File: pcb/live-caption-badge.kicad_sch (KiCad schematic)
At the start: 35 parts, among them J1 Conn_01x09, J2 Conn_01x04_Socket, J3 Conn_01x09, J5 USB_C_Receptacle_USB2.0_16P, J6 Conn_01x06, J7 Conn_01x03, SW1 SW_DPDT_x2, SW2 RST, SW3 BTN, SW4 BTN, SW5 BTN, U1 ESP32-S3-WROOM-1, U2 HE9073A33M5R, U3 HE9073A33M5R

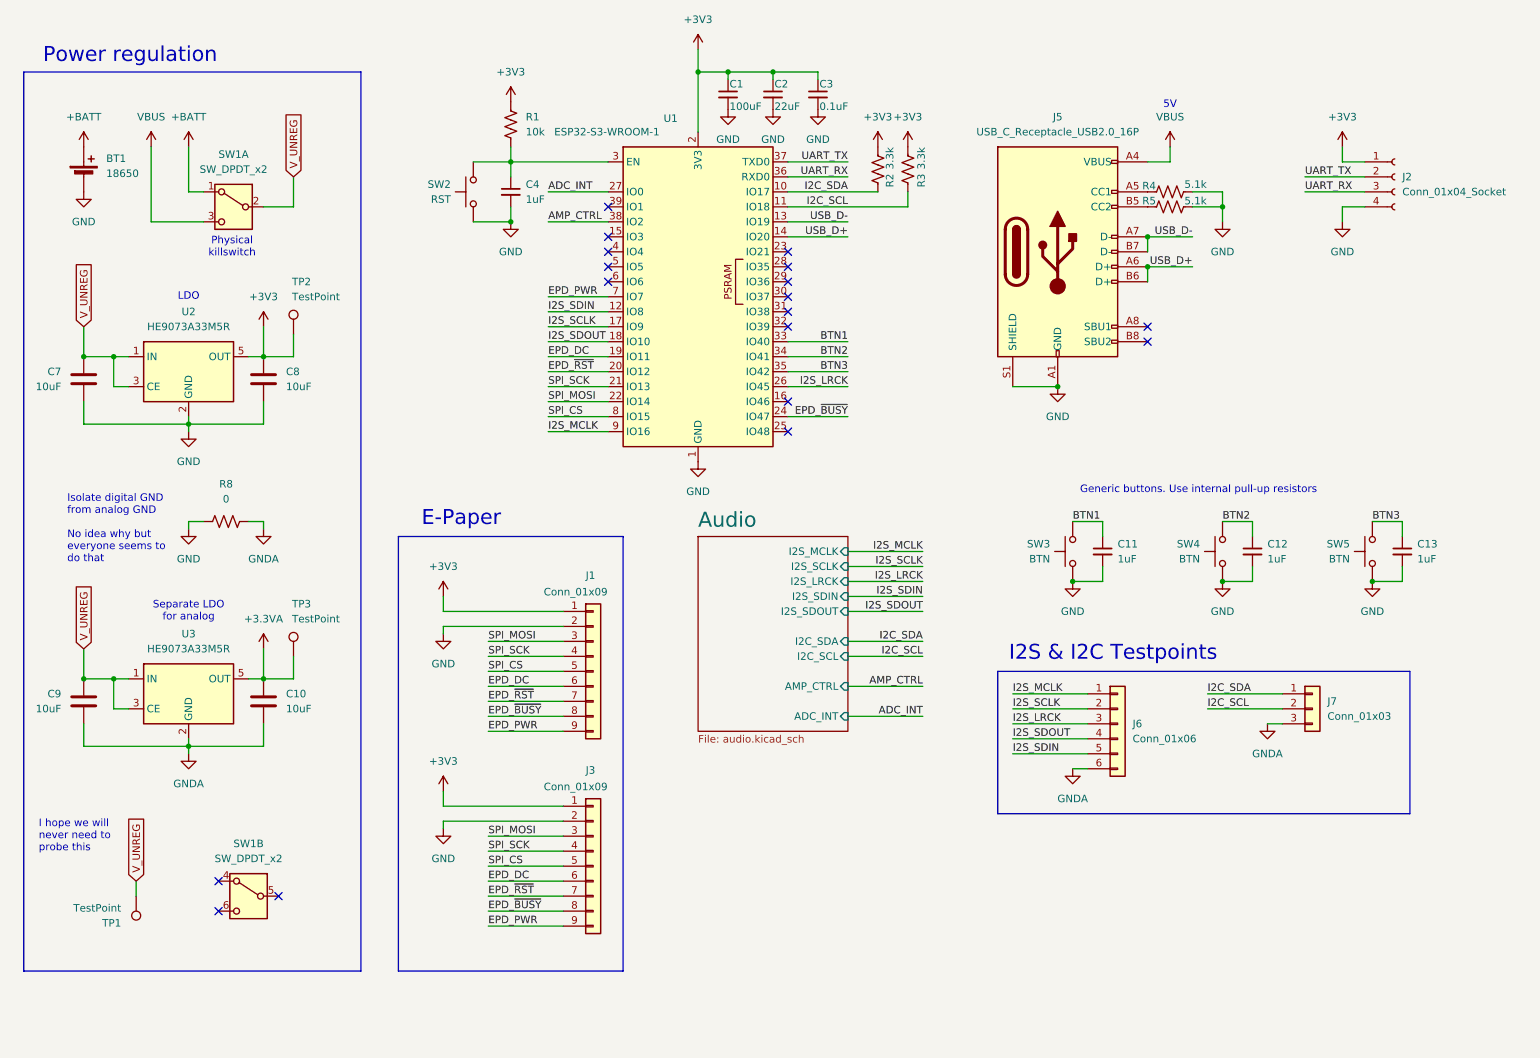
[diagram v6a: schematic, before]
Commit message: pcb: Convert to 4-layer board
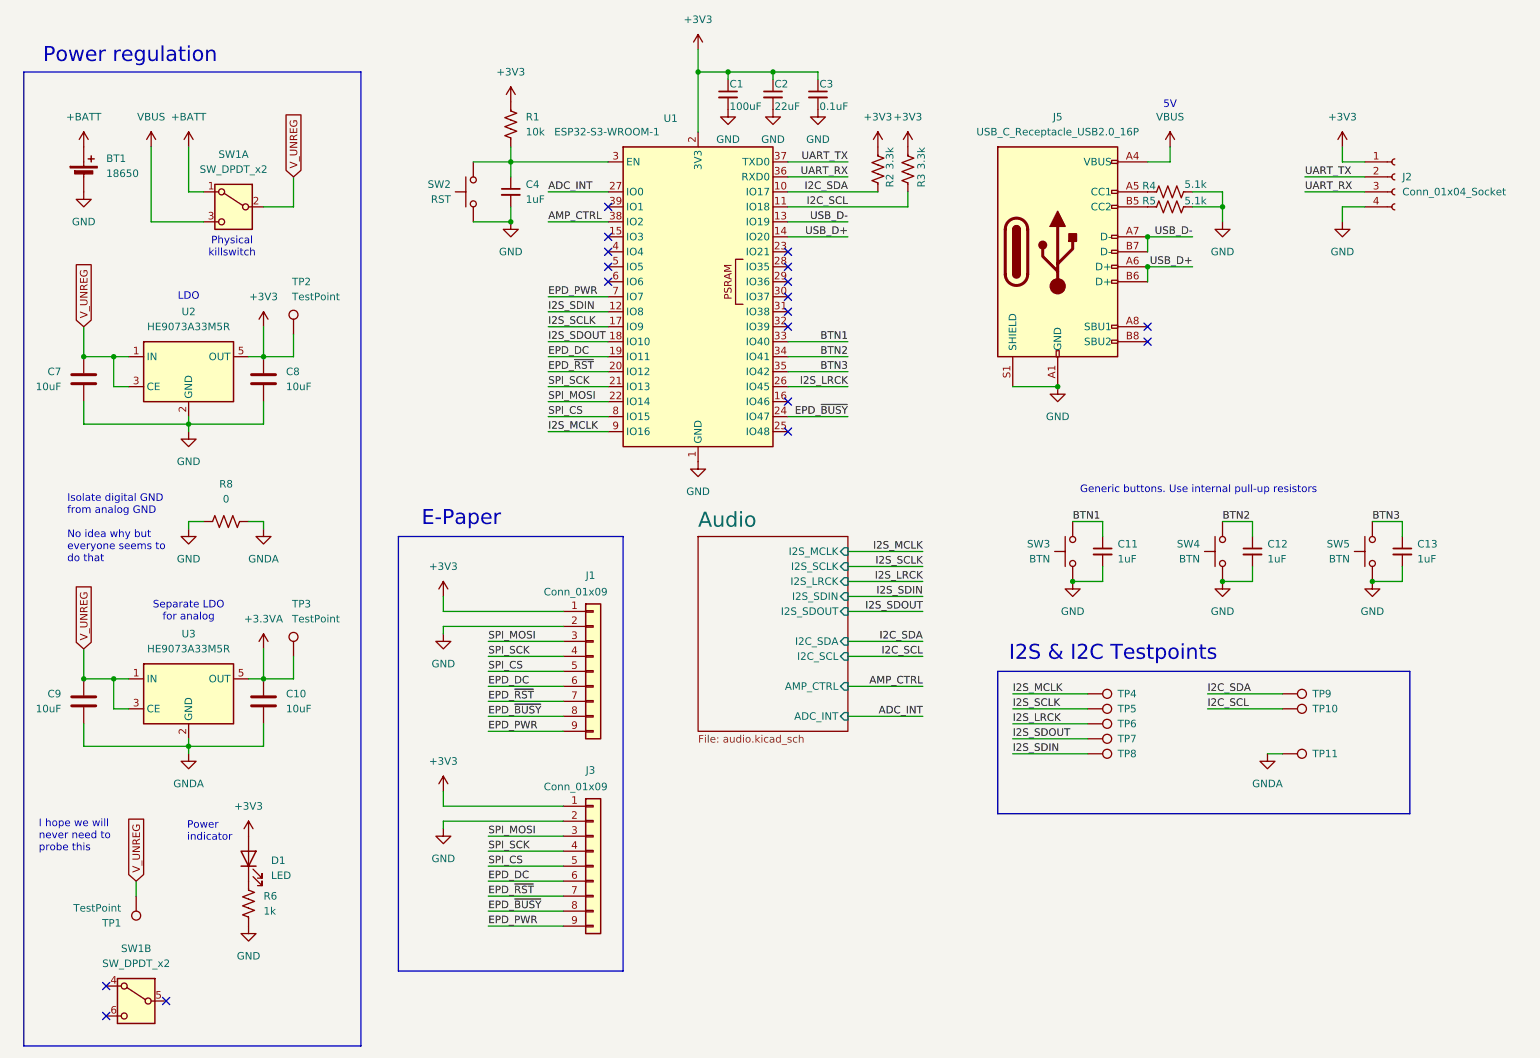
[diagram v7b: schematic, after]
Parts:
- removed J6: Conn_01x06, Connector_PinHeader_2.54mm:PinHeader_1x06_P2.54mm_Vertical, symbol Connector_Generic:Conn_01x06
- removed J7: Conn_01x03, Connector_PinHeader_2.54mm:PinHeader_1x03_P2.54mm_Vertical, symbol Connector_Generic:Conn_01x03
- added D1: LED, LED_SMD:LED_0603_1608Metric, symbol Device:LED
- added R6: 1k, Resistor_SMD:R_0603_1608Metric, symbol Device:R_US
- added TP10, TP11, TP4, TP5, TP6, TP7, TP8, TP9: TestPoint, Connector_PinHeader_2.54mm:PinHeader_1x01_P2.54mm_Vertical, symbol Connector:TestPoint
- U1: footprint RF_Module:ESP32-S3-WROOM-1 -> live-caption-badge:ESP32-S3-WROOM-1-LargerVias
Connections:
- net +3V3: now also D1.2 (A)
- net GND: now also R6.1
- net GNDA: now also TP11.1
- net I2C_SCL: now also TP10.1
- net I2C_SDA: now also TP9.1
- net I2S_LRCK: now also TP6.1
- net I2S_MCLK: now also TP4.1
- net I2S_SCLK: now also TP5.1
- net I2S_SDIN: now also TP8.1
- net I2S_SDOUT: now also TP7.1
- new net: D1.1 (K), R6.2
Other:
- note added: "Power indicator"
- moved on the sheet: SW1B

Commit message: pcb: it may or may not work
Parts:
- removed J2: Conn_01x04_Socket, Connector_PinSocket_2.54mm:PinSocket_1x04_P2.54mm_Vertical, symbol Connector:Conn_01x04_Socket
- added C5: 1uF, Capacitor_SMD:C_0603_1608Metric, symbol Device:C_Small
- added J2: Conn_01x06, Connector_PinHeader_2.54mm:PinHeader_1x06_P2.54mm_Vertical, symbol Connector_Generic:Conn_01x06
- added R13, R14: 0, Resistor_SMD:R_0603_1608Metric, symbol Device:R_US
- added SW6: RST, live-caption-badge:SW_Push_6x3mm, symbol Switch:SW_Push
- J1: footprint Connector_Molex:Molex_CLIK-Mate_502386-0970_1x09-1MP_P1.25mm_Horizontal -> live-caption-badge:Molex_CLIK-Mate_502386-0970_1x09-1MP_P1.25mm_Horizontal
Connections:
- net +3V3: now also J2.1 (Pin_1)
- net ADC_INT: now also U1.31 (IO38); no longer U1.27 (IO0)
- net GND: now also C5.2, J2.6 (Pin_6), SW6.1
- net UART_RX: now also J2.3 (Pin_3)
- net UART_TX: now also J2.2 (Pin_2)
- net USB_D+: now also R14.1; no longer U1.14 (IO20)
- net USB_D-: now also R13.1; no longer U1.13 (IO19)
- net ESP_EN: now reaches C4.1, R1.2, SW2.2, U1.3 (EN)
- net ESP_EN: now also J2.5 (Pin_5)
- new net ESP_D+: R14.2, U1.14 (IO20)
- new net ESP_D-: R13.2, U1.13 (IO19)
- new net ESP_IO0: C5.1, J2.4 (Pin_4), SW6.2, U1.27 (IO0)
- no-connect marks 18 -> 17
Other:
- moved on the sheet: C4, J5, R1, R4, R5, SW2, TP10, TP4, TP5, TP6, TP7, TP8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
